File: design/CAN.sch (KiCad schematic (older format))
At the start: 4 parts, among them U401 SN65HVD232

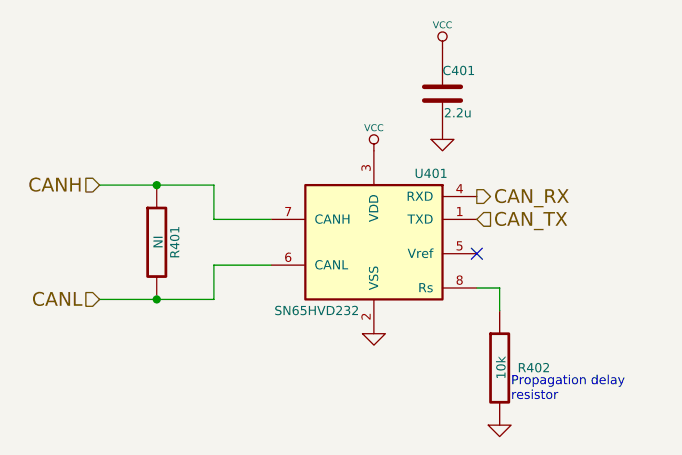
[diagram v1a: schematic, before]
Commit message: Make change in annotations and some small fixes
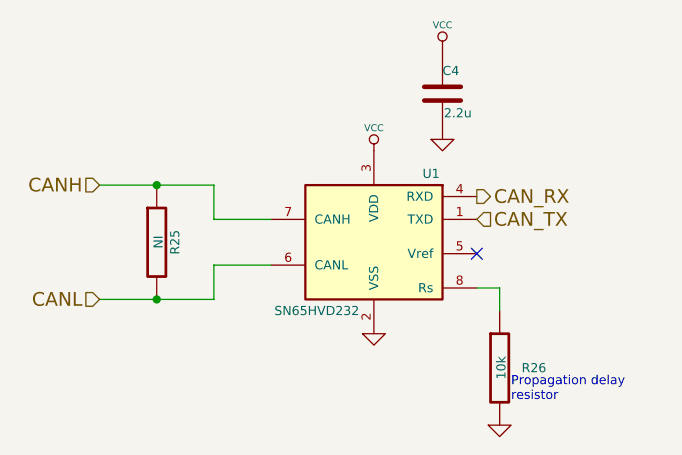
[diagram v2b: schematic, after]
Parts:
- renumbered C401 to C4, R401 to R25, R402 to R26, U401 to U1
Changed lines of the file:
@@
 $Descr A4 11693 8268
 encoding utf-8
-Sheet 4 11
+Sheet 4 10
 Title "CAN BUS transceiver"
-Date "13 jan 2015"
+Date "16 jan 2015"
 Rev ""
 Comp "Mrk Industries"
@@
 $EndDescr
 $Comp
-L MCP2551-I/SN U401
+L MCP2551-I/SN U1
 U 1 1 53F59F90
 P 5850 4050
-F 0 "U401" H 5600 4350 40  0000 C CNN
+F 0 "U1" H 5600 4350 40  0000 C CNN
 F 1 "SN65HVD232" H 6100 3750 40  0000 C CNN
 F 2 "SMD_Packages:SOIC-8-W" H 5850 4050 35  0001 C CIN
@@
 $EndComp
 $Comp
-L GND #PWR025
+L GND #PWR030
 U 1 1 53F59F97
 P 5850 4450
-F 0 "#PWR025" H 5850 4450 30  0001 C CNN
+F 0 "#PWR030" H 5850 4450 30  0001 C CNN
 F 1 "GND" H 5850 4380 30  0001 C CNN
 F 2 "" H 5850 4450 60  0000 C CNN
@@
 $EndComp
 $Comp
-L VCC #PWR026
+L VCC #PWR031
 U 1 1 53F59F9D
 P 5850 3650
-F 0 "#PWR026" H 5850 3750 30  0001 C CNN
+F 0 "#PWR031" H 5850 3750 30  0001 C CNN
 F 1 "VCC" H 5850 3750 30  0000 C CNN
 F 2 "" H 5850 3650 60  0001 C CNN
@@
 $EndComp
 $Comp
-L C C401
+L C C4
 U 1 1 53F59FA3
 P 6150 3400
-F 0 "C401" H 6150 3500 40  0000 L CNN
+F 0 "C4" H 6150 3500 40  0000 L CNN
 F 1 "2.2u" H 6156 3315 40  0000 L CNN
 F 2 "SMD_Packages:SMD-0402" H 6188 3250 30  0001 C CNN
@@
 $EndComp
 $Comp
-L VCC #PWR027
+L VCC #PWR032
 U 1 1 53F59FAA
 P 6150 3200
-F 0 "#PWR027" H 6150 3300 30  0001 C CNN
+F 0 "#PWR032" H 6150 3300 30  0001 C CNN
 F 1 "VCC" H 6150 3300 30  0000 C CNN
 F 2 "" H 6150 3200 60  0001 C CNN
@@
 $EndComp
 $Comp
-L GND #PWR028
+L GND #PWR033
 U 1 1 53F59FB0
 P 6150 3600
-F 0 "#PWR028" H 6150 3600 30  0001 C CNN
+F 0 "#PWR033" H 6150 3600 30  0001 C CNN
 F 1 "GND" H 6150 3530 30  0001 C CNN
 F 2 "" H 6150 3600 60  0000 C CNN
@@
 CAN_TX
 $Comp
-L R R401
+L R R25
 U 1 1 540030A8
 P 4900 4050
-F 0 "R401" V 4980 4050 40  0000 C CNN
+F 0 "R25" V 4980 4050 40  0000 C CNN
 F 1 "NI" V 4907 4051 40  0000 C CNN
 F 2 "SMD_Packages:SMD-0603_r" V 4830 4050 30  0001 C CNN
@@
 NoConn ~ 6300 4100
 $Comp
-L R R402
+L R R26
 U 1 1 54003136
 P 6400 4600
-F 0 "R402" H 6550 4600 40  0000 C CNN
+F 0 "R26" H 6550 4600 40  0000 C CNN
 F 1 "10k" V 6407 4601 40  0000 C CNN
 F 2 "SMD_Packages:SMD-0603_r" V 6330 4600 30  0001 C CNN
@@
 	6400 4250 6300 4250
 $Comp
-L GND #PWR029
+L GND #PWR034
 U 1 1 5400318B
 P 6400 4850
-F 0 "#PWR029" H 6400 4850 30  0001 C CNN
+F 0 "#PWR034" H 6400 4850 30  0001 C CNN
 F 1 "GND" H 6400 4780 30  0001 C CNN
 F 2 "" H 6400 4850 60  0000 C CNN
